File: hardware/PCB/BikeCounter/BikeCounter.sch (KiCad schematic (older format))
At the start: 5 parts

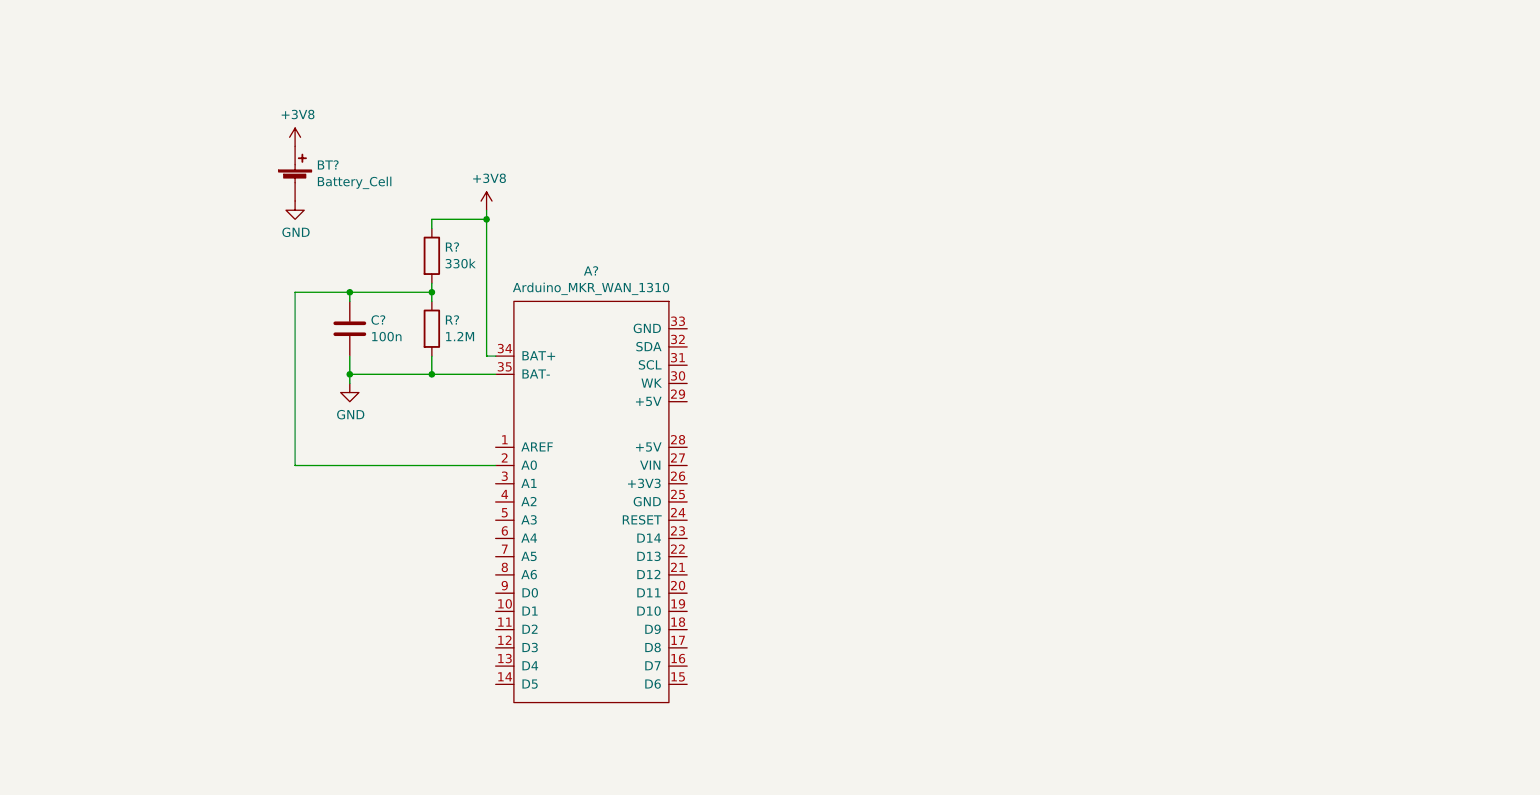
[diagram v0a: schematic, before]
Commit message: First version of circuit diagram finished
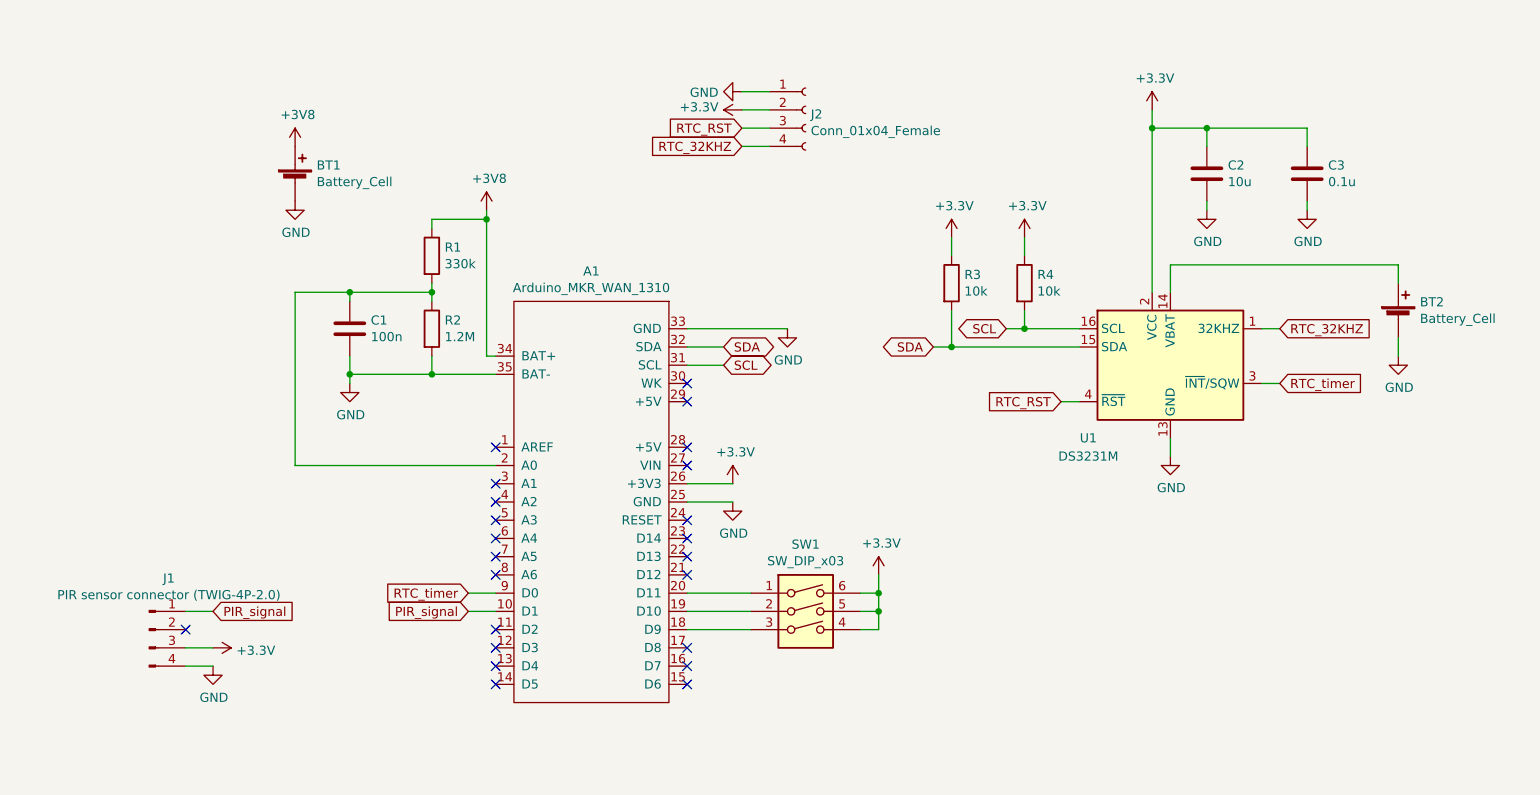
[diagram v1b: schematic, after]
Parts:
- added BT2: Battery_Cell, symbol Device:Battery_Cell
- added C2: 10u, symbol Device:C
- added C3: 0.1u, symbol Device:C
- added J1: PIR sensor connector (TWIG-4P-2.0), symbol Connector:Conn_01x04_Male
- added J2: Conn_01x04_Female, Connector_PinSocket_2.54mm:PinSocket_1x04_P2.54mm_Vertical, symbol Connector:Conn_01x04_Female
- added R3, R4: 10k, symbol Device:R
- added SW1: SW_DIP_x03, symbol Switch:SW_DIP_x03
- added U1: DS3231M, Package_SO:SOIC-16W_7.5x10.3mm_P1.27mm, symbol Timer_RTC:DS3231M
- BT1: renamed from BT?; footprint (none) -> Battery:BatteryHolder_Keystone_1042_1x18650
- gave numbers to parts that had none: 4
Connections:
- net GND: now also A1.25 (GND), A1.33 (GND), BT2.2 (-), C2.2, C3.2, J1.4 (Pin_4), J2.1 (Pin_1), U1.10 (GND), U1.11 (GND), U1.12 (GND), U1.13 (GND), U1.5 (GND), U1.6 (GND), U1.7 (GND), U1.8 (GND), U1.9 (GND)
- net PIR_signal: now reaches A1.10 (D1)
- net PIR_signal: now also J1.1 (Pin_1)
- net at A1.18 (D9): now also SW1.3
- net at A1.19 (D10): now also SW1.2
- net at A1.20 (D11): now also SW1.1
- net +3V3: now reaches A1.26 (+3V3)
- net +3V3: now also C2.1, C3.1, J1.3 (Pin_3), J2.2 (Pin_2), R3.1, R4.1, SW1.4, SW1.5, SW1.6, U1.2 (VCC)
- net SCL: now reaches A1.31 (SCL)
- net SCL: now also R4.2, U1.16 (SCL)
- net SDA: now reaches A1.32 (SDA)
- net SDA: now also R3.2, U1.15 (SDA)
- net RTC_timer: now reaches A1.9 (D0)
- net RTC_timer: now also U1.3 (~INT~/SQW)
- new net: BT2.1 (+), U1.14 (VBAT)
- new net RTC_32KHZ: J2.4 (Pin_4), U1.1 (32KHZ)
- new net RTC_RST: J2.3 (Pin_3), U1.4 (~RST)
- no-connect marks 0 -> 23

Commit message: PCB v0.1 finished
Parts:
- added J3: Conn_01x02_Female, Connector_PinSocket_2.54mm:PinSocket_1x02_P2.54mm_Vertical, symbol Connector:Conn_01x02_Female
- added R5, R6, R7: 10k, Resistor_SMD:R_1206_3216Metric_Pad1.42x1.75mm_HandSolder, symbol Device:R
- BT2: footprint (none) -> Battery:BatteryHolder_Keystone_3000_1x12mm
- C1: value 100n -> 0.1uF; footprint (none) -> Capacitor_SMD:C_0805_2012Metric_Pad1.15x1.40mm_HandSolder
- C2: value 10u -> 10uF; footprint (none) -> Capacitor_SMD:C_1206_3216Metric_Pad1.33x1.80mm_HandSolder
- C3: value 0.1u -> 0.1uF; footprint (none) -> Capacitor_SMD:C_0805_2012Metric_Pad1.15x1.40mm_HandSolder
- J1: footprint (none) -> Connector_PinSocket_2.00mm:PinSocket_1x04_P2.00mm_Vertical
- R1, R2, R3, R4: footprint (none) -> Resistor_SMD:R_1206_3216Metric_Pad1.42x1.75mm_HandSolder
- SW1: footprint (none) -> Button_Switch_SMD:SW_DIP_SPSTx03_Slide_6.7x9.18mm_W8.61mm_P2.54mm_LowProfile
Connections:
- net +3V8: now also J3.1 (Pin_1); no longer A1.34 (BAT+)
- net GND: now also J3.2 (Pin_2), R5.2, R6.2, R7.2; no longer A1.33 (GND), A1.35 (BAT-)
- net SCL: now also A1.21 (D12); no longer A1.31 (SCL)
- net SDA: now also A1.20 (D11); no longer A1.32 (SDA)
- net at A1.17 (D8): now also SW1.3, R7.1
- net at A1.18 (D9): now also SW1.2, R6.1; no longer SW1.3
- net at A1.19 (D10): now also SW1.1, R5.1; no longer SW1.2
- no-connect marks 23 -> 27
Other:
- moved on the sheet: BT1, C1, R1, R2, SW1
